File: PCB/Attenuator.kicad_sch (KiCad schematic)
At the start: 55 parts, among them J1 In, J2 Out, J3 I2C, K1 G6K-2, K2 G6K-2, K3 G6K-2, K4 G6K-2, K5 G6K-2, K6 G6K-2, K7 G6K-2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

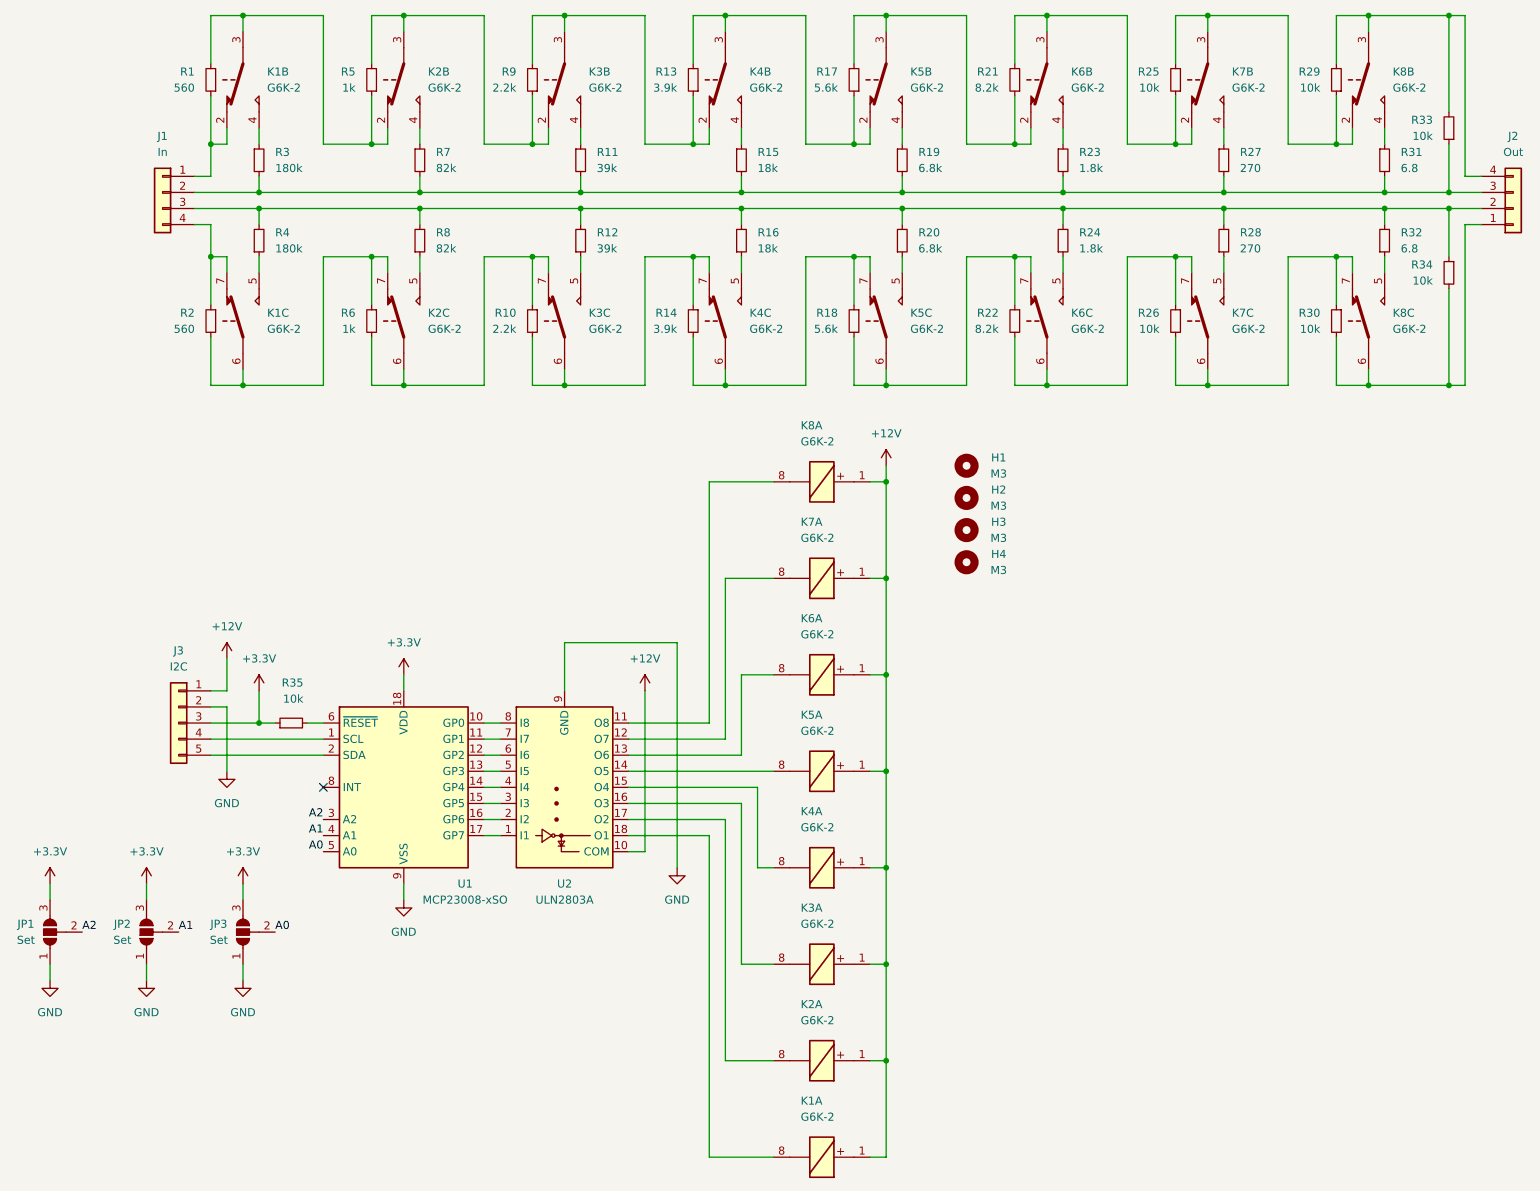
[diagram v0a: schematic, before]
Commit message: Added 1u decoupling capacitors to ICs on backplane and attenuator boards
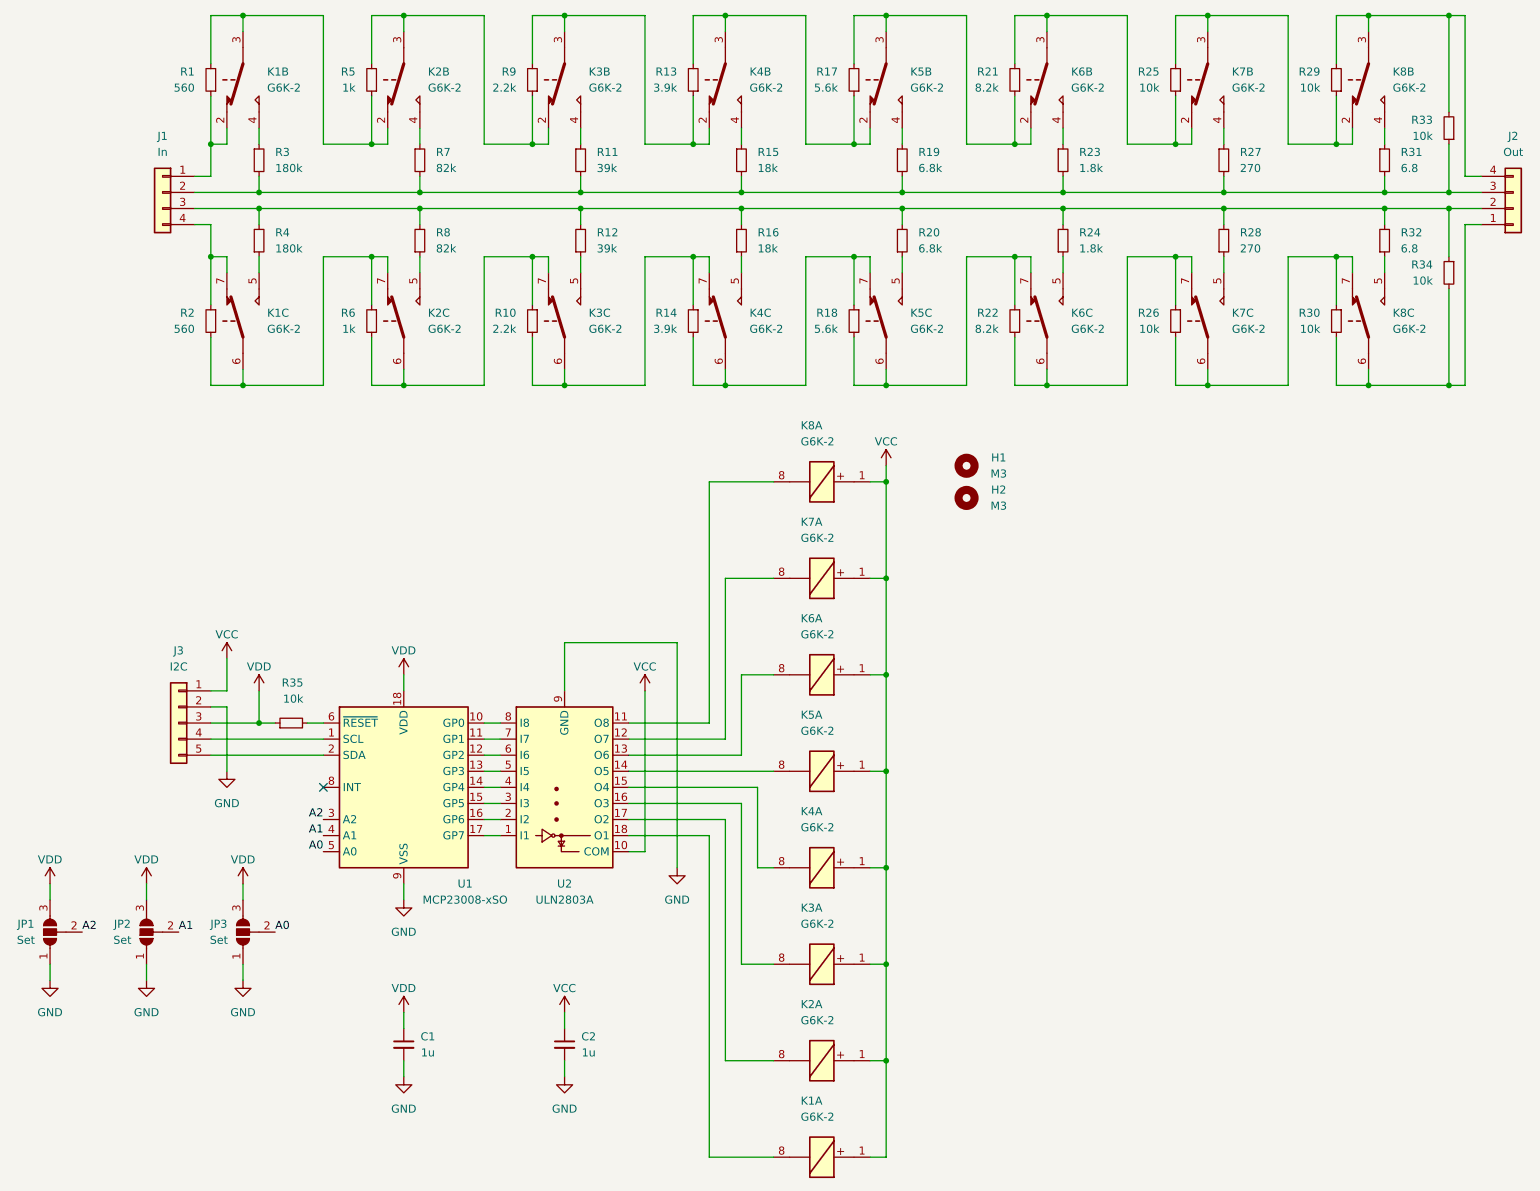
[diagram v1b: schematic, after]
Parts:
- removed H3, H4: M3, MountingHole:MountingHole_3.2mm_M3_DIN965_Pad, symbol Mechanical:MountingHole
- added C1, C2: 1u, Capacitor_SMD:C_0603_1608Metric, symbol Device:C_Small
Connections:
- net GND: now also C1.2, C2.2
- net +12V renamed VCC
- net VCC: now also C2.1
- net +3V3 renamed VDD
- net VDD: now also C1.1

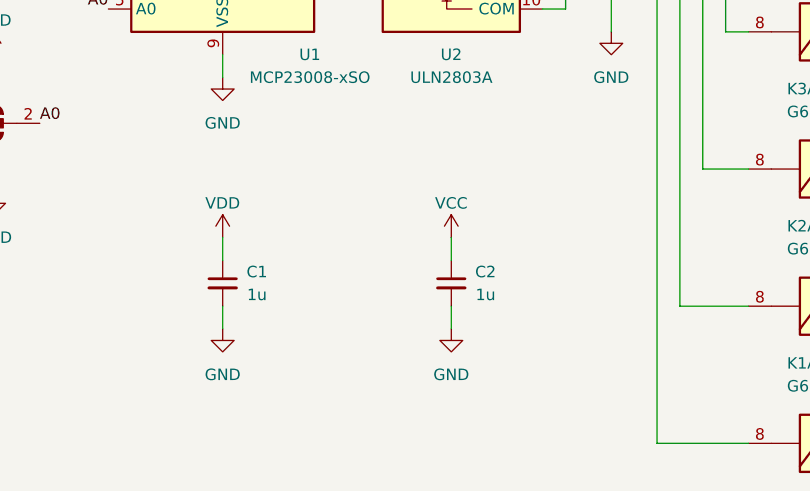
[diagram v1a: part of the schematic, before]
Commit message: Added bulk capacitance to each IC, rerouted 5V line on backplane board
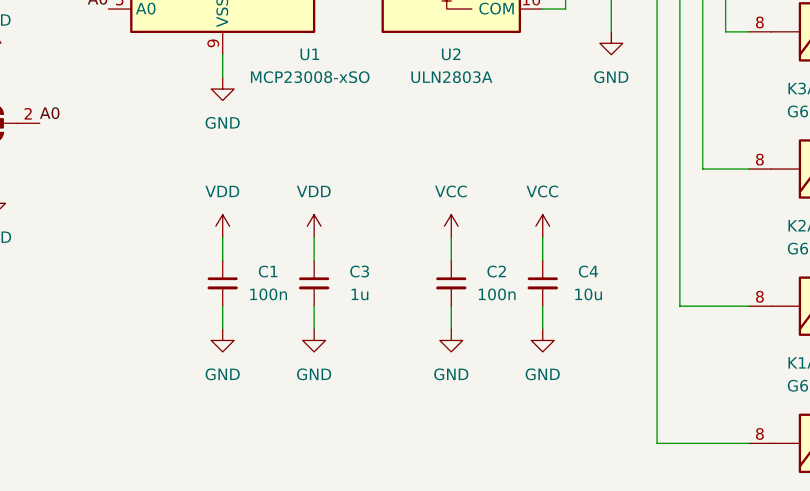
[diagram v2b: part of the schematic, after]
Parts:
- added C3: 1u, Capacitor_SMD:C_0603_1608Metric, symbol Device:C_Small
- added C4: 10u, Capacitor_SMD:C_0603_1608Metric, symbol Device:C_Small
- C1, C2: value 1u -> 100n
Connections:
- net GND: now also C3.2, C4.2
- net VCC: now also C4.1
- net VDD: now also C3.1
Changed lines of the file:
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@@
+    (stroke (width 0) (type default) (color 0 0 0 0))
+  )
+  (wire (pts (xy 116.84 170.18) (xy 116.84 172.72))
     (stroke (width 0) (type default) (color 0 0 0 0))
   )
@@
     (stroke (width 0) (type default) (color 0 0 0 0))
   )
+  (wire (pts (xy 91.44 177.8) (xy 91.44 180.34))
+    (stroke (width 0) (type default) (color 0 0 0 0))
+  )
   (wire (pts (xy 106.68 71.12) (xy 106.68 68.58))
     (stroke (width 0) (type default) (color 0 0 0 0))
@@
     (stroke (width 0) (type default) (color 0 0 0 0))
   )
+  (wire (pts (xy 116.84 177.8) (xy 116.84 180.34))
+    (stroke (width 0) (type default) (color 0 0 0 0))
+  )
   (wire (pts (xy 170.18 71.12) (xy 170.18 50.8))
     (stroke (width 0) (type default) (color 0 0 0 0))
@@
   )
   (wire (pts (xy 195.58 71.12) (xy 195.58 50.8))
+    (stroke (width 0) (type default) (color 0 0 0 0))
+  )
+  (wire (pts (xy 91.44 170.18) (xy 91.44 172.72))
     (stroke (width 0) (type default) (color 0 0 0 0))
   )
@@
   (symbol (lib_id "Device:C_Small") (at 81.28 175.26 0) (mirror y) (unit 1)
     (in_bom yes) (on_board yes) (fields_autoplaced)
-    (property "Reference" "C1" (id 0) (at 85.09 173.9962 0))
-    (property "Value" "1u" (id 1) (at 85.09 176.5362 0))
+    (property "Reference" "C1" (id 0) (at 86.36 173.9962 0))
+    (property "Value" "100n" (id 1) (at 86.36 176.5362 0))
     (property "Footprint" "Capacitor_SMD:C_0603_1608Metric" (id 2) (at 81.28 175.26 0)
       (effects (font (size 1.27 1.27)) hide)
@@
     (pin "1")
   )
+  (symbol (lib_id "power:VCC") (at 116.84 170.18 0) (unit 1)
+    (in_bom yes) (on_board yes) (fields_autoplaced)
+    (property "Reference" "#PWR0119" (id 0) (at 116.84 173.99 0)
+      (effects (font (size 1.27 1.27)) hide)
+    )
+    (property "Value" "VCC" (id 1) (at 116.84 165.1 0))
+    (property "Footprint" "" (id 2) (at 116.84 170.18 0)
+      (effects (font (size 1.27 1.27)) hide)
+    )
+    (property "Datasheet" "" (id 3) (at 116.84 170.18 0)
+      (effects (font (size 1.27 1.27)) hide)
+    )
+    (pin "1")
+  )
   (symbol (lib_id "power:VDD") (at 58.42 119.38 0) (unit 1)
     (in_bom yes) (on_board yes)
@@
   )
   (symbol (lib_id "power:VDD") (at 81.28 170.18 0) (unit 1)
-    (in_bom yes) (on_board yes)
+    (in_bom yes) (on_board yes) (fields_autoplaced)
     (property "Reference" "#PWR0114" (id 0) (at 81.28 173.99 0)
       (effects (font (size 1.27 1.27)) hide)
     )
-    (property "Value" "VDD" (id 1) (at 81.28 166.37 0))
+    (property "Value" "VDD" (id 1) (at 81.28 165.1 0))
     (property "Footprint" "" (id 2) (at 81.28 170.18 0)
       (effects (font (size 1.27 1.27)) hide)
@@
   (symbol (lib_id "Device:C_Small") (at 106.68 175.26 0) (mirror y) (unit 1)
     (in_bom yes) (on_board yes) (fields_autoplaced)
-    (property "Reference" "C2" (id 0) (at 110.49 173.9962 0))
-    (property "Value" "1u" (id 1) (at 110.49 176.5362 0))
+    (property "Reference" "C2" (id 0) (at 111.76 173.9962 0))
+    (property "Value" "100n" (id 1) (at 111.76 176.5362 0))
     (property "Footprint" "Capacitor_SMD:C_0603_1608Metric" (id 2) (at 106.68 175.26 0)
       (effects (font (size 1.27 1.27)) hide)
@@
     (pin "6")
     (pin "7")
+  )
+  (symbol (lib_id "power:VDD") (at 91.44 170.18 0) (unit 1)
+    (in_bom yes) (on_board yes) (fields_autoplaced)
+    (property "Reference" "#PWR0122" (id 0) (at 91.44 173.99 0)
+      (effects (font (size 1.27 1.27)) hide)
+    )
+    (property "Value" "VDD" (id 1) (at 91.44 165.1 0))
+    (property "Footprint" "" (id 2) (at 91.44 170.18 0)
+      (effects (font (size 1.27 1.27)) hide)
+    )
+    (property "Datasheet" "" (id 3) (at 91.44 170.18 0)
+      (effects (font (size 1.27 1.27)) hide)
+    )
+    (pin "1")
   )
   (symbol (lib_id "Device:R_Small") (at 177.8 22.86 180) (unit 1)
@@
     (pin "9")
   )
+  (symbol (lib_id "Device:C_Small") (at 91.44 175.26 0) (mirror y) (unit 1)
+    (in_bom yes) (on_board yes) (fields_autoplaced)
+    (property "Reference" "C3" (id 0) (at 96.52 173.9962 0))
+    (property "Value" "1u" (id 1) (at 96.52 176.5362 0))
+    (property "Footprint" "Capacitor_SMD:C_0603_1608Metric" (id 2) (at 91.44 175.26 0)
+      (effects (font (size 1.27 1.27)) hide)
+    )
+    (property "Datasheet" "~" (id 3) (at 91.44 175.26 0)
+      (effects (font (size 1.27 1.27)) hide)
+    )
+    (property "LCSC part number" "C15849" (id 4) (at 91.44 175.26 0)
+      (effects (font (size 1.27 1.27)) hide)
+    )
+    (property "Part number" "CL10A105KB8NNNC" (id 5) (at 91.44 175.26 0)
+      (effects (font (size 1.27 1.27)) hide)
+    )
+    (pin "1")
+    (pin "2")
+  )
   (symbol (lib_id "Device:R_Small") (at 160.02 35.56 0) (unit 1)
     (in_bom yes) (on_board yes) (fields_autoplaced)
@@
     (pin "1")
   )
+  (symbol (lib_id "Device:C_Small") (at 116.84 175.26 0) (mirror y) (unit 1)
+    (in_bom yes) (on_board yes) (fields_autoplaced)
+    (property "Reference" "C4" (id 0) (at 121.92 173.9962 0))
+    (property "Value" "10u" (id 1) (at 121.92 176.5362 0))
+    (property "Footprint" "Capacitor_SMD:C_0603_1608Metric" (id 2) (at 116.84 175.26 0)
+      (effects (font (size 1.27 1.27)) hide)
+    )
+    (property "Datasheet" "~" (id 3) (at 116.84 175.26 0)
+      (effects (font (size 1.27 1.27)) hide)
+    )
+    (property "LCSC part number" "C15849" (id 4) (at 116.84 175.26 0)
+      (effects (font (size 1.27 1.27)) hide)
+    )
+    (property "Part number" "CL10A105KB8NNNC" (id 5) (at 116.84 175.26 0)
+      (effects (font (size 1.27 1.27)) hide)
+    )
+    (pin "1")
+    (pin "2")
+  )
   (symbol (lib_id "Device:R_Small") (at 50.8 22.86 180) (unit 1)
     (in_bom yes) (on_board yes) (fields_autoplaced)
@@
   )
   (symbol (lib_id "power:VCC") (at 106.68 170.18 0) (unit 1)
-    (in_bom yes) (on_board yes)
+    (in_bom yes) (on_board yes) (fields_autoplaced)
     (property "Reference" "#PWR0116" (id 0) (at 106.68 173.99 0)
       (effects (font (size 1.27 1.27)) hide)
     )
-    (property "Value" "VCC" (id 1) (at 106.68 166.37 0))
+    (property "Value" "VCC" (id 1) (at 106.68 165.1 0))
     (property "Footprint" "" (id 2) (at 106.68 170.18 0)
       (effects (font (size 1.27 1.27)) hide)
     )
     (property "Datasheet" "" (id 3) (at 106.68 170.18 0)
+      (effects (font (size 1.27 1.27)) hide)
+    )
+    (pin "1")
+  )
+  (symbol (lib_id "power:GND") (at 91.44 180.34 0) (mirror y) (unit 1)
+    (in_bom yes) (on_board yes) (fields_autoplaced)
+    (property "Reference" "#PWR0120" (id 0) (at 91.44 186.69 0)
+      (effects (font (size 1.27 1.27)) hide)
+    )
+    (property "Value" "GND" (id 1) (at 91.44 185.42 0))
+    (property "Footprint" "" (id 2) (at 91.44 180.34 0)
+      (effects (font (size 1.27 1.27)) hide)
+    )
+    (property "Datasheet" "" (id 3) (at 91.44 180.34 0)
       (effects (font (size 1.27 1.27)) hide)
     )
@@
     )
   )
+  (symbol (lib_id "power:GND") (at 116.84 180.34 0) (mirror y) (unit 1)
+    (in_bom yes) (on_board yes) (fields_autoplaced)
+    (property "Reference" "#PWR0121" (id 0) (at 116.84 186.69 0)
+      (effects (font (size 1.27 1.27)) hide)
+    )
+    (property "Value" "GND" (id 1) (at 116.84 185.42 0))
+    (property "Footprint" "" (id 2) (at 116.84 180.34 0)
+      (effects (font (size 1.27 1.27)) hide)
+    )
+    (property "Datasheet" "" (id 3) (at 116.84 180.34 0)
+      (effects (font (size 1.27 1.27)) hide)
+    )
+    (pin "1")
+  )
   (symbol (lib_id "Omicron:G6K-2_Separated") (at 55.88 60.96 0) (unit 3)
     (in_bom yes) (on_board yes) (fields_autoplaced)
@@
       (reference "#PWR0118") (unit 1) (value "VCC") (footprint "")
     )
+    (path "/459b036d-0fde-43a8-9bcf-7e2c885957e8"
+      (reference "#PWR0119") (unit 1) (value "VCC") (footprint "")
+    )
+    (path "/e2a9c1bf-5319-4be0-88ae-c6de8400213d"
+      (reference "#PWR0120") (unit 1) (value "GND") (footprint "")
+    )
+    (path "/f3101cee-363a-4a6a-8db3-7131c233334f"
+      (reference "#PWR0121") (unit 1) (value "GND") (footprint "")
+    )
+    (path "/a2b655f8-d5cf-4ef4-ba08-3b39b3bb945e"
+      (reference "#PWR0122") (unit 1) (value "VDD") (footprint "")
+    )
     (path "/07e014ba-ca34-4ee3-906c-68c38f33eb08"
-      (reference "C1") (unit 1) (value "1u") (footprint "Capacitor_SMD:C_0603_1608Metric")
+      (reference "C1") (unit 1) (value "100n") (footprint "Capacitor_SMD:C_0603_1608Metric")
     )
     (path "/73b4ca9d-3ef0-4bcc-869e-f4ccffe74cba"
-      (reference "C2") (unit 1) (value "1u") (footprint "Capacitor_SMD:C_0603_1608Metric")
+      (reference "C2") (unit 1) (value "100n") (footprint "Capacitor_SMD:C_0603_1608Metric")
+    )
+    (path "/b40c5ed9-1eee-4769-87f5-ec43f5c54044"
+      (reference "C3") (unit 1) (value "1u") (footprint "Capacitor_SMD:C_0603_1608Metric")
+    )
+    (path "/bbafbf97-2ca0-43a7-8b2c-074bed245bc9"
+      (reference "C4") (unit 1) (value "10u") (footprint "Capacitor_SMD:C_0603_1608Metric")
     )
     (path "/edcdfea8-5352-46be-bec0-b6826a87c632"
